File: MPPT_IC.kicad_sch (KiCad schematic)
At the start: 1 part

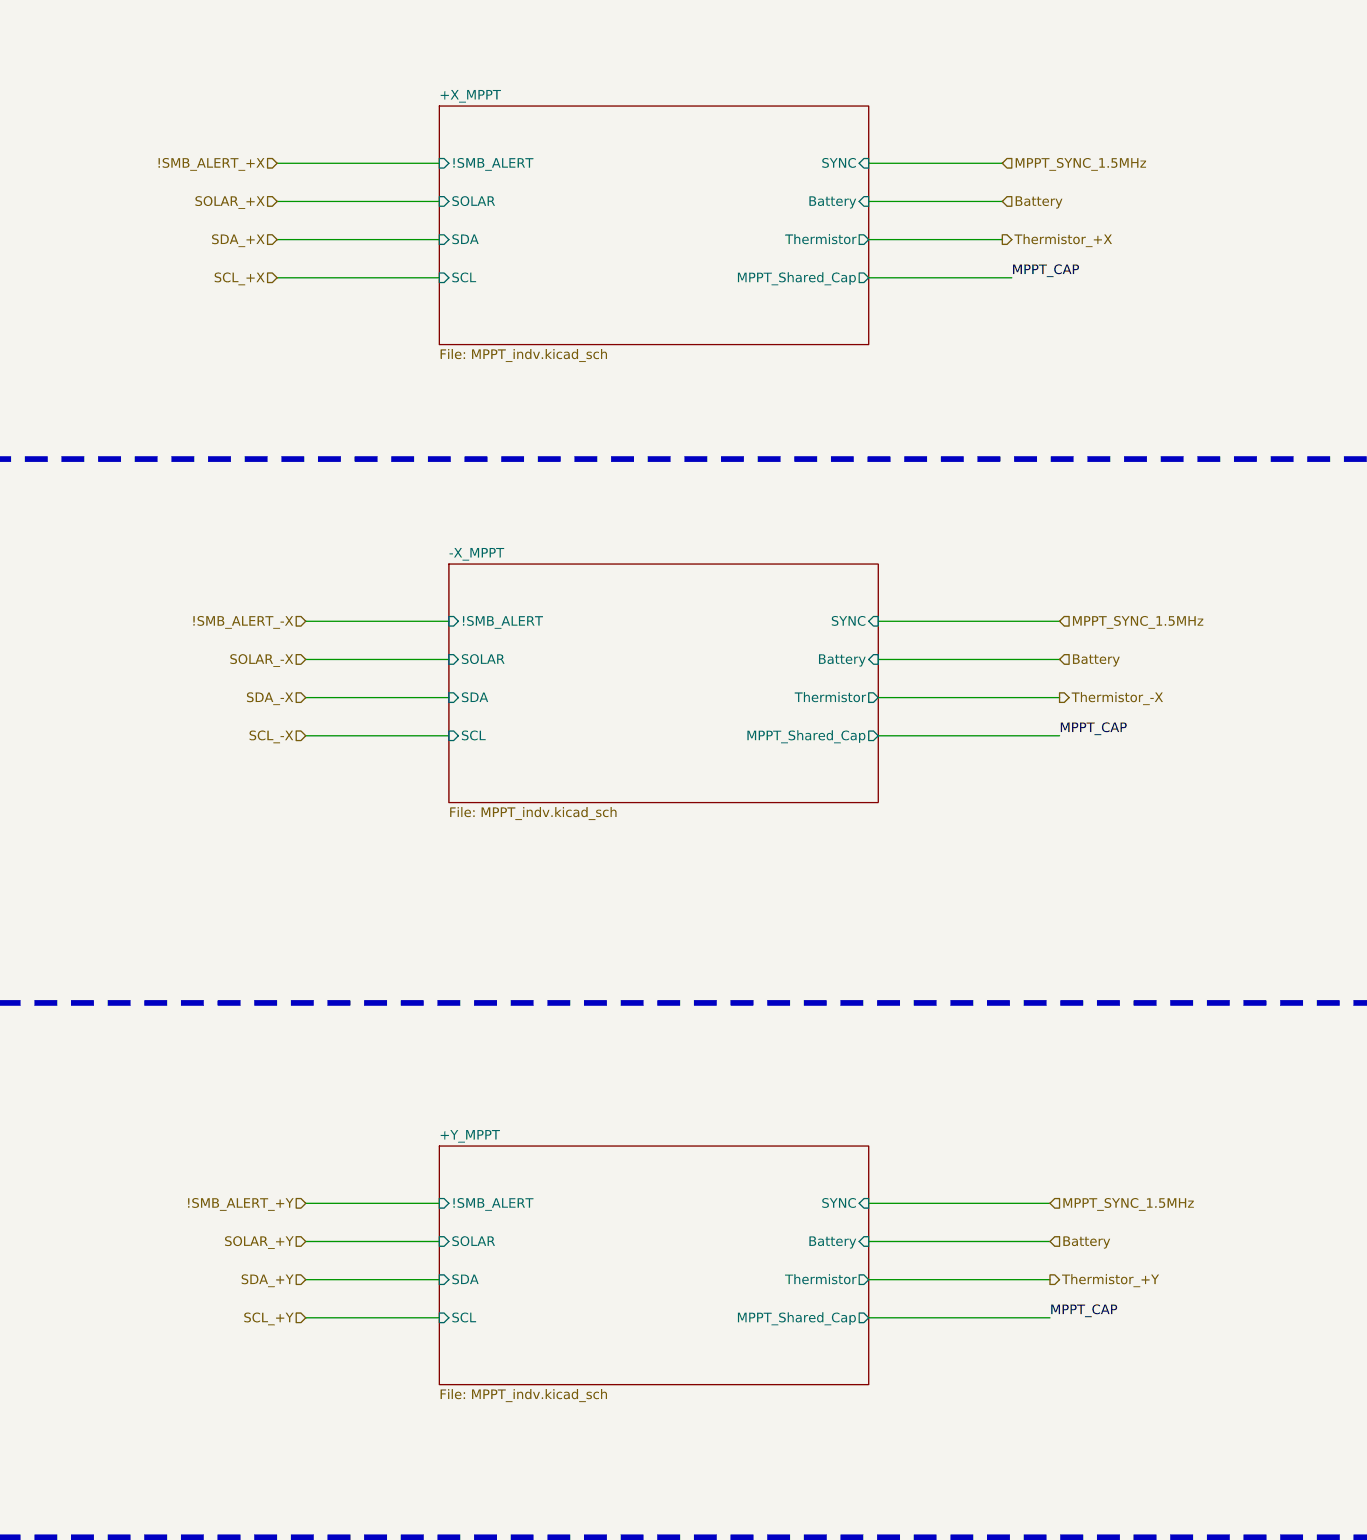
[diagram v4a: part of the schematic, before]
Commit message: Small schematic changes
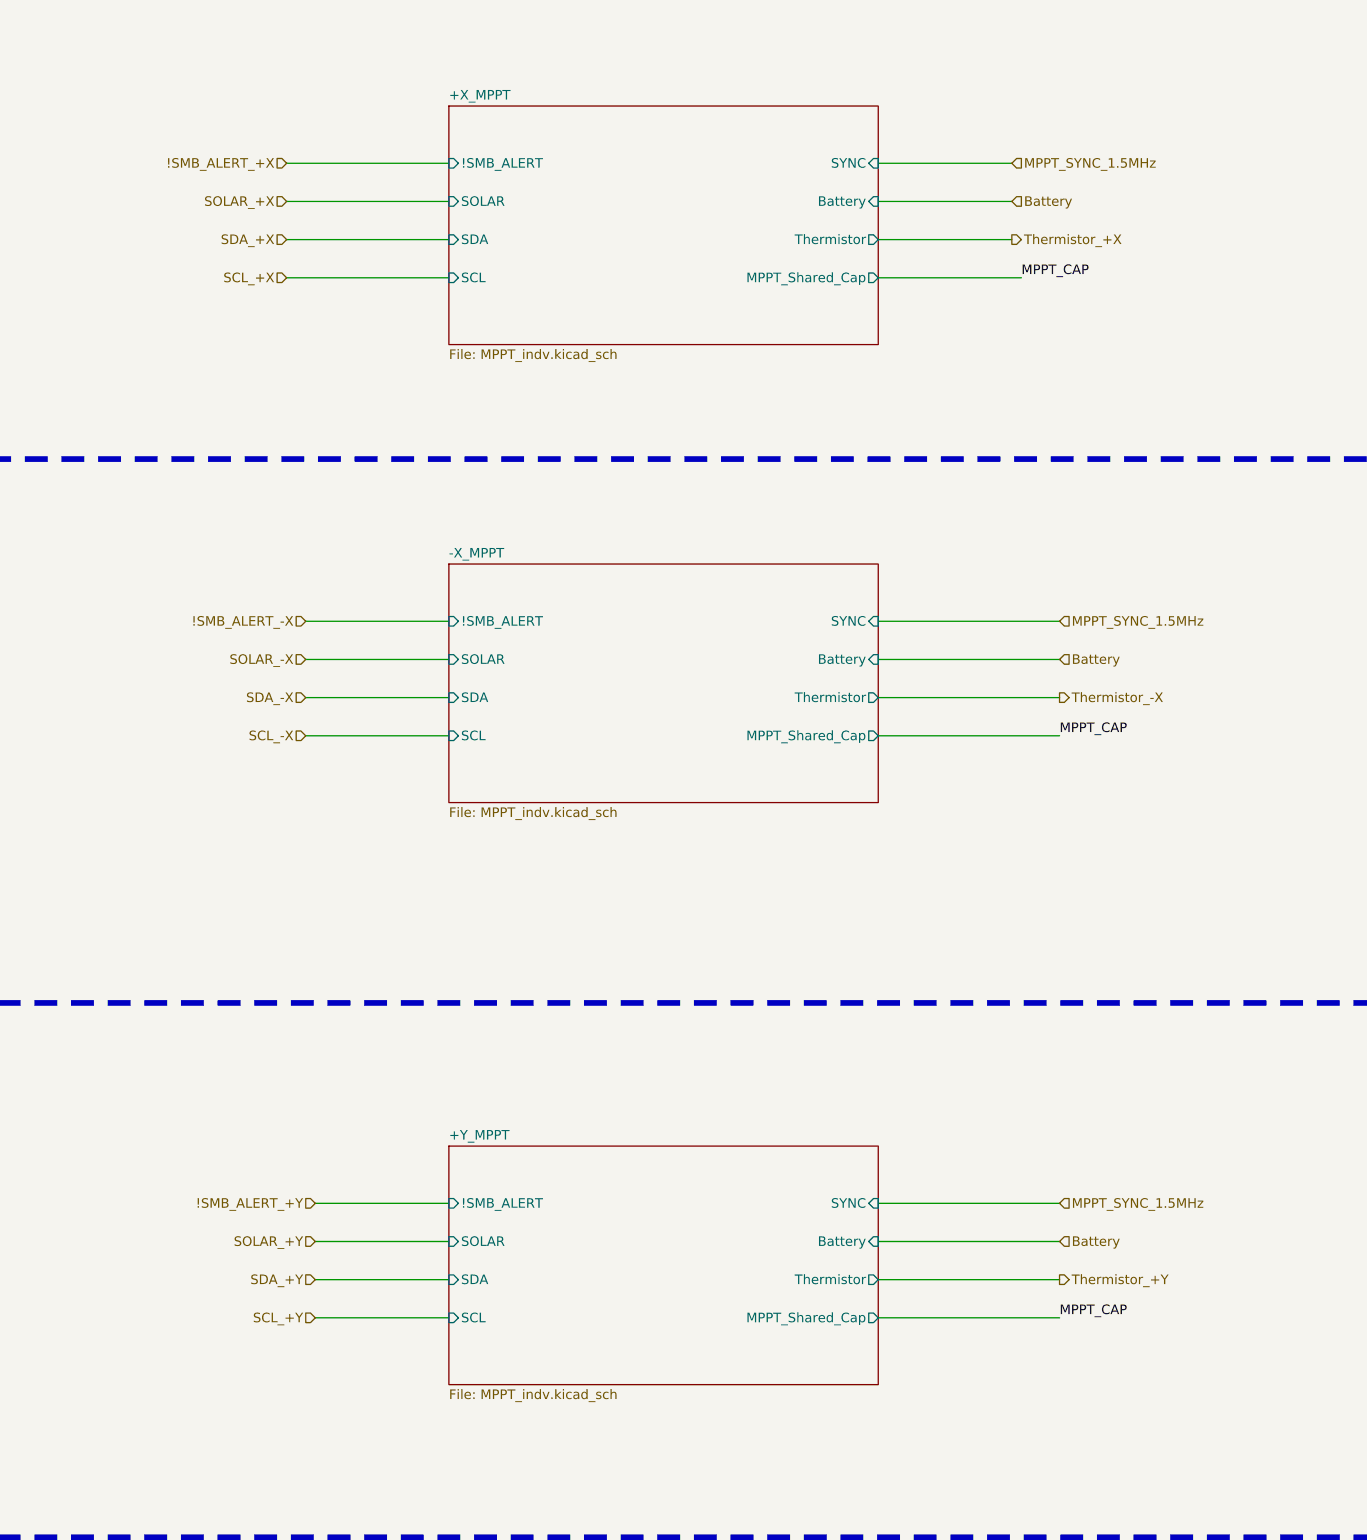
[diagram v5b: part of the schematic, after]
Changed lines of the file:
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@@
 	(wire
 		(pts
-			(xy 90.17 48.26) (xy 111.76 48.26)
-		)
-		(stroke
-			(width 0)
-			(type default)
-		)
-	)
-	(wire
-		(pts
-			(xy 93.98 171.45) (xy 111.76 171.45)
-		)
-		(stroke
-			(width 0)
-			(type default)
-		)
-	)
-	(wire
-		(pts
-			(xy 168.91 38.1) (xy 186.69 38.1)
-		)
-		(stroke
-			(width 0)
-			(type default)
-		)
-	)
-	(wire
-		(pts
-			(xy 93.98 186.69) (xy 111.76 186.69)
+			(xy 91.44 48.26) (xy 113.03 48.26)
+		)
+		(stroke
+			(width 0)
+			(type default)
+		)
+	)
+	(wire
+		(pts
+			(xy 95.25 171.45) (xy 113.03 171.45)
+		)
+		(stroke
+			(width 0)
+			(type default)
+		)
+	)
+	(wire
+		(pts
+			(xy 170.18 38.1) (xy 187.96 38.1)
+		)
+		(stroke
+			(width 0)
+			(type default)
+		)
+	)
+	(wire
+		(pts
+			(xy 95.25 186.69) (xy 113.03 186.69)
 		)
 		(stroke
@@
 	(wire
 		(pts
-			(xy 193.04 186.69) (xy 168.91 186.69)
+			(xy 194.31 186.69) (xy 170.18 186.69)
 		)
 		(stroke
@@
 	(wire
 		(pts
-			(xy 193.04 171.45) (xy 168.91 171.45)
+			(xy 194.31 171.45) (xy 170.18 171.45)
 		)
 		(stroke
@@
 	(wire
 		(pts
-			(xy 93.98 176.53) (xy 111.76 176.53)
+			(xy 95.25 176.53) (xy 113.03 176.53)
 		)
 		(stroke
@@
 	(wire
 		(pts
-			(xy 186.69 33.02) (xy 168.91 33.02)
+			(xy 187.96 33.02) (xy 170.18 33.02)
 		)
 		(stroke
@@
 	(wire
 		(pts
-			(xy 93.98 181.61) (xy 111.76 181.61)
-		)
-		(stroke
-			(width 0)
-			(type default)
-		)
-	)
-	(wire
-		(pts
-			(xy 193.04 176.53) (xy 168.91 176.53)
-		)
-		(stroke
-			(width 0)
-			(type default)
-		)
-	)
-	(wire
-		(pts
-			(xy 168.91 43.18) (xy 186.69 43.18)
-		)
-		(stroke
-			(width 0)
-			(type default)
-		)
-	)
-	(wire
-		(pts
-			(xy 90.17 43.18) (xy 111.76 43.18)
+			(xy 95.25 181.61) (xy 113.03 181.61)
+		)
+		(stroke
+			(width 0)
+			(type default)
+		)
+	)
+	(wire
+		(pts
+			(xy 194.31 176.53) (xy 170.18 176.53)
+		)
+		(stroke
+			(width 0)
+			(type default)
+		)
+	)
+	(wire
+		(pts
+			(xy 170.18 43.18) (xy 187.96 43.18)
+		)
+		(stroke
+			(width 0)
+			(type default)
+		)
+	)
+	(wire
+		(pts
+			(xy 91.44 43.18) (xy 113.03 43.18)
 		)
 		(stroke
@@
 	(wire
 		(pts
-			(xy 168.91 48.26) (xy 187.96 48.26)
-		)
-		(stroke
-			(width 0)
-			(type default)
-		)
-	)
-	(wire
-		(pts
-			(xy 90.17 33.02) (xy 111.76 33.02)
-		)
-		(stroke
-			(width 0)
-			(type default)
-		)
-	)
-	(wire
-		(pts
-			(xy 90.17 38.1) (xy 111.76 38.1)
+			(xy 170.18 48.26) (xy 189.23 48.26)
+		)
+		(stroke
+			(width 0)
+			(type default)
+		)
+	)
+	(wire
+		(pts
+			(xy 91.44 33.02) (xy 113.03 33.02)
+		)
+		(stroke
+			(width 0)
+			(type default)
+		)
+	)
+	(wire
+		(pts
+			(xy 91.44 38.1) (xy 113.03 38.1)
 		)
 		(stroke
@@
 	(wire
 		(pts
-			(xy 193.04 181.61) (xy 168.91 181.61)
+			(xy 194.31 181.61) (xy 170.18 181.61)
 		)
 		(stroke
@@
 	)
 	(label "MPPT_CAP"
-		(at 187.96 48.26 0)
+		(at 189.23 48.26 0)
 		(effects
 			(font
@@
 	)
 	(label "MPPT_CAP"
-		(at 193.04 186.69 0)
+		(at 194.31 186.69 0)
 		(effects
 			(font
@@
 	(hierarchical_label "SDA_+X"
 		(shape input)
-		(at 90.17 43.18 180)
+		(at 91.44 43.18 180)
 		(effects
 			(font
@@
 	(hierarchical_label "MPPT_SYNC_1.5MHz"
 		(shape input)
-		(at 186.69 33.02 0)
+		(at 187.96 33.02 0)
 		(effects
 			(font
@@
 	(hierarchical_label "Thermistor_+Y"
 		(shape output)
-		(at 193.04 181.61 0)
+		(at 194.31 181.61 0)
 		(effects
 			(font
@@
 	(hierarchical_label "SCL_+Y"
 		(shape input)
-		(at 93.98 186.69 180)
+		(at 95.25 186.69 180)
 		(effects
 			(font
@@
 	(hierarchical_label "SDA_+Y"
 		(shape input)
-		(at 93.98 181.61 180)
+		(at 95.25 181.61 180)
 		(effects
 			(font
@@
 	(hierarchical_label "Battery"
 		(shape input)
-		(at 186.69 38.1 0)
+		(at 187.96 38.1 0)
 		(effects
 			(font
@@
 	(hierarchical_label "MPPT_SYNC_1.5MHz"
 		(shape input)
-		(at 193.04 171.45 0)
+		(at 194.31 171.45 0)
 		(effects
 			(font
@@
 	(hierarchical_label "!SMB_ALERT_+X"
 		(shape input)
-		(at 90.17 33.02 180)
+		(at 91.44 33.02 180)
 		(effects
 			(font
@@
 	(hierarchical_label "Battery"
 		(shape input)
-		(at 193.04 176.53 0)
+		(at 194.31 176.53 0)
 		(effects
 			(font
@@
 	(hierarchical_label "SOLAR_+Y"
 		(shape input)
-		(at 93.98 176.53 180)
+		(at 95.25 176.53 180)
 		(effects
 			(font
@@
 	(hierarchical_label "Thermistor_+X"
 		(shape output)
-		(at 186.69 43.18 0)
+		(at 187.96 43.18 0)
 		(effects
 			(font
@@
 	(hierarchical_label "SCL_+X"
 		(shape input)
-		(at 90.17 48.26 180)
+		(at 91.44 48.26 180)
 		(effects
 			(font
@@
 	(hierarchical_label "!SMB_ALERT_+Y"
 		(shape input)
-		(at 93.98 171.45 180)
+		(at 95.25 171.45 180)
 		(effects
 			(font
@@
 	(hierarchical_label "SOLAR_+X"
 		(shape input)
-		(at 90.17 38.1 180)
+		(at 91.44 38.1 180)
 		(effects
 			(font
@@
 	)
 	(sheet
-		(at 111.76 163.83)
+		(at 113.03 163.83)
 		(size 57.15 31.75)
 		(exclude_from_sim no)
@@
 		)
 		(property "Sheetname" "+Y_MPPT"
-			(at 111.76 163.1184 0)
+			(at 113.03 163.1184 0)
 			(effects
 				(font
@@
 		)
 		(property "Sheetfile" "MPPT_indv.kicad_sch"
-			(at 111.76 196.1646 0)
+			(at 113.03 196.1646 0)
 			(effects
 				(font
@@
 		)
 		(pin "SOLAR" input
-			(at 111.76 176.53 180)
+			(at 113.03 176.53 180)
 			(effects
 				(font
@@
 		)
 		(pin "SDA" input
-			(at 111.76 181.61 180)
+			(at 113.03 181.61 180)
 			(effects
 				(font
@@
 		)
 		(pin "Battery" input
-			(at 168.91 176.53 0)
+			(at 170.18 176.53 0)
 			(effects
 				(font
@@
 		)
 		(pin "Thermistor" output
-			(at 168.91 181.61 0)
+			(at 170.18 181.61 0)
 			(effects
 				(font
@@
 		)
 		(pin "SCL" input
-			(at 111.76 186.69 180)
+			(at 113.03 186.69 180)
 			(effects
 				(font
@@
 		)
 		(pin "!SMB_ALERT" input
-			(at 111.76 171.45 180)
+			(at 113.03 171.45 180)
 			(effects
 				(font
@@
 		)
 		(pin "MPPT_Shared_Cap" output
-			(at 168.91 186.69 0)
+			(at 170.18 186.69 0)
 			(effects
 				(font
@@
 		)
 		(pin "SYNC" input
-			(at 168.91 171.45 0)
+			(at 170.18 171.45 0)
 			(effects
 				(font
@@
 	)
 	(sheet
-		(at 111.76 25.4)
+		(at 113.03 25.4)
 		(size 57.15 31.75)
 		(exclude_from_sim no)
@@
 		)
 		(property "Sheetname" "+X_MPPT"
-			(at 111.76 24.6884 0)
+			(at 113.03 24.6884 0)
 			(effects
 				(font
@@
 		)
 		(property "Sheetfile" "MPPT_indv.kicad_sch"
-			(at 111.76 57.7346 0)
+			(at 113.03 57.7346 0)
 			(effects
 				(font
@@
 		)
 		(pin "SOLAR" input
-			(at 111.76 38.1 180)
+			(at 113.03 38.1 180)
 			(effects
 				(font
@@
 		)
 		(pin "SDA" input
-			(at 111.76 43.18 180)
+			(at 113.03 43.18 180)
 			(effects
 				(font
@@
 		)
 		(pin "Battery" input
-			(at 168.91 38.1 0)
+			(at 170.18 38.1 0)
 			(effects
 				(font
@@
 		)
 		(pin "Thermistor" output
-			(at 168.91 43.18 0)
+			(at 170.18 43.18 0)
 			(effects
 				(font
@@
 		)
 		(pin "SCL" input
-			(at 111.76 48.26 180)
+			(at 113.03 48.26 180)
 			(effects
 				(font
@@
 		)
 		(pin "!SMB_ALERT" input
-			(at 111.76 33.02 180)
+			(at 113.03 33.02 180)
 			(effects
 				(font
@@
 		)
 		(pin "MPPT_Shared_Cap" output
-			(at 168.91 48.26 0)
+			(at 170.18 48.26 0)
 			(effects
 				(font
@@
 		)
 		(pin "SYNC" input
-			(at 168.91 33.02 0)
-			(effects
-				(font
+			(at 170.18 33.02 0)
+			(effects
+				(font
